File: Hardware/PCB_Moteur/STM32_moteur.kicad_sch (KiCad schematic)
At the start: 66 parts, among them J2 Conn_01x06_Pin, U2 STM32F103CBT6

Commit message: wip: new pressure et fix alim
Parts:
- removed R59: 22R, Resistor_SMD:R_0603_1608Metric, symbol Device:R_Small
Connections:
- no-connect marks 2 -> 3
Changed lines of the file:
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@@
 	)
 	(no_connect
+		(at 133.35 72.39)
+	)
+	(no_connect
 		(at 133.35 95.25)
 	)
@@
 	(wire
 		(pts
-			(xy 125.73 72.39) (xy 127 72.39)
-		)
-		(stroke
-			(width 0)
-			(type default)
-		)
-	)
-	(wire
-		(pts
 			(xy 243.84 35.56) (xy 251.46 35.56)
 		)
@@
 	(wire
 		(pts
-			(xy 132.08 72.39) (xy 133.35 72.39)
-		)
-		(stroke
-			(width 0)
-			(type default)
-		)
-	)
-	(wire
-		(pts
 			(xy 148.59 127) (xy 151.13 127)
 		)
@@
 		)
 	)
-	(global_label "Pressure_Sleep"
-		(shape input)
-		(at 125.73 72.39 180)
-		(fields_autoplaced yes)
-		(effects
-			(font
-				(size 1.27 1.27)
-			)
-			(justify right)
-		)
-		(property "Intersheetrefs" "${INTERSHEET_REFS}"
-			(at 108.3515 72.39 0)
-			(effects
-				(font
-					(size 1.27 1.27)
-				)
-				(justify right)
-				(hide yes)
-			)
-		)
-	)
 	(global_label "Servo3_Close"
 		(shape input)
@@
 					(unit 1)
 				)
-			)
-		)
-	)
-	(symbol
-		(lib_id "Device:R_Small")
-		(at 129.54 72.39 90)
-		(unit 1)
-		(exclude_from_sim no)
-		(in_bom yes)
-		(on_board yes)
-		(dnp no)
-		(property "Reference" "R59"
-			(at 102.87 72.39 90)
-			(effects
-				(font
-					(size 1.016 1.016)
-				)
-				(justify left)
-			)
-		)
-		(property "Value" "22R"
-			(at 99.314 72.39 90)
-			(effects
-				(font
-					(size 1.27 1.27)
-				)
-				(justify left)
-			)
-		)
-		(property "Footprint" "Resistor_SMD:R_0603_1608Metric"
-			(at 129.54 72.39 0)
-			(effects
-				(font
-					(size 1.27 1.27)
-				)
-				(hide yes)
-			)
-		)
-		(property "Datasheet" "~"
-			(at 129.54 72.39 0)
-			(effects
-				(font
-					(size 1.27 1.27)
-				)
-				(hide yes)
-			)
-		)
-		(property "Description" "Resistor, small symbol"
-			(at 129.54 72.39 0)
-			(effects
-				(font
-					(size 1.27 1.27)
-				)
-				(hide yes)
-			)
-		)
-		(pin "1"
-		)
-		(pin "2"
-		)
-		(instances
-			(project "PCB_moteur"
-				(path "/b0d87684-7b1c-41d8-8358-755aa327573e/753d1783-c2f5-4012-bbb8-3f4eadf066f6"
-					(reference "R59")
-					(unit 1)
-				)
-			)
-			(project "STM32_moteur"
-				(path "/da6e3e70-7434-4a0f-acc5-62316b7258e2"
-					(reference "R?")
-					(unit 1)
-				)

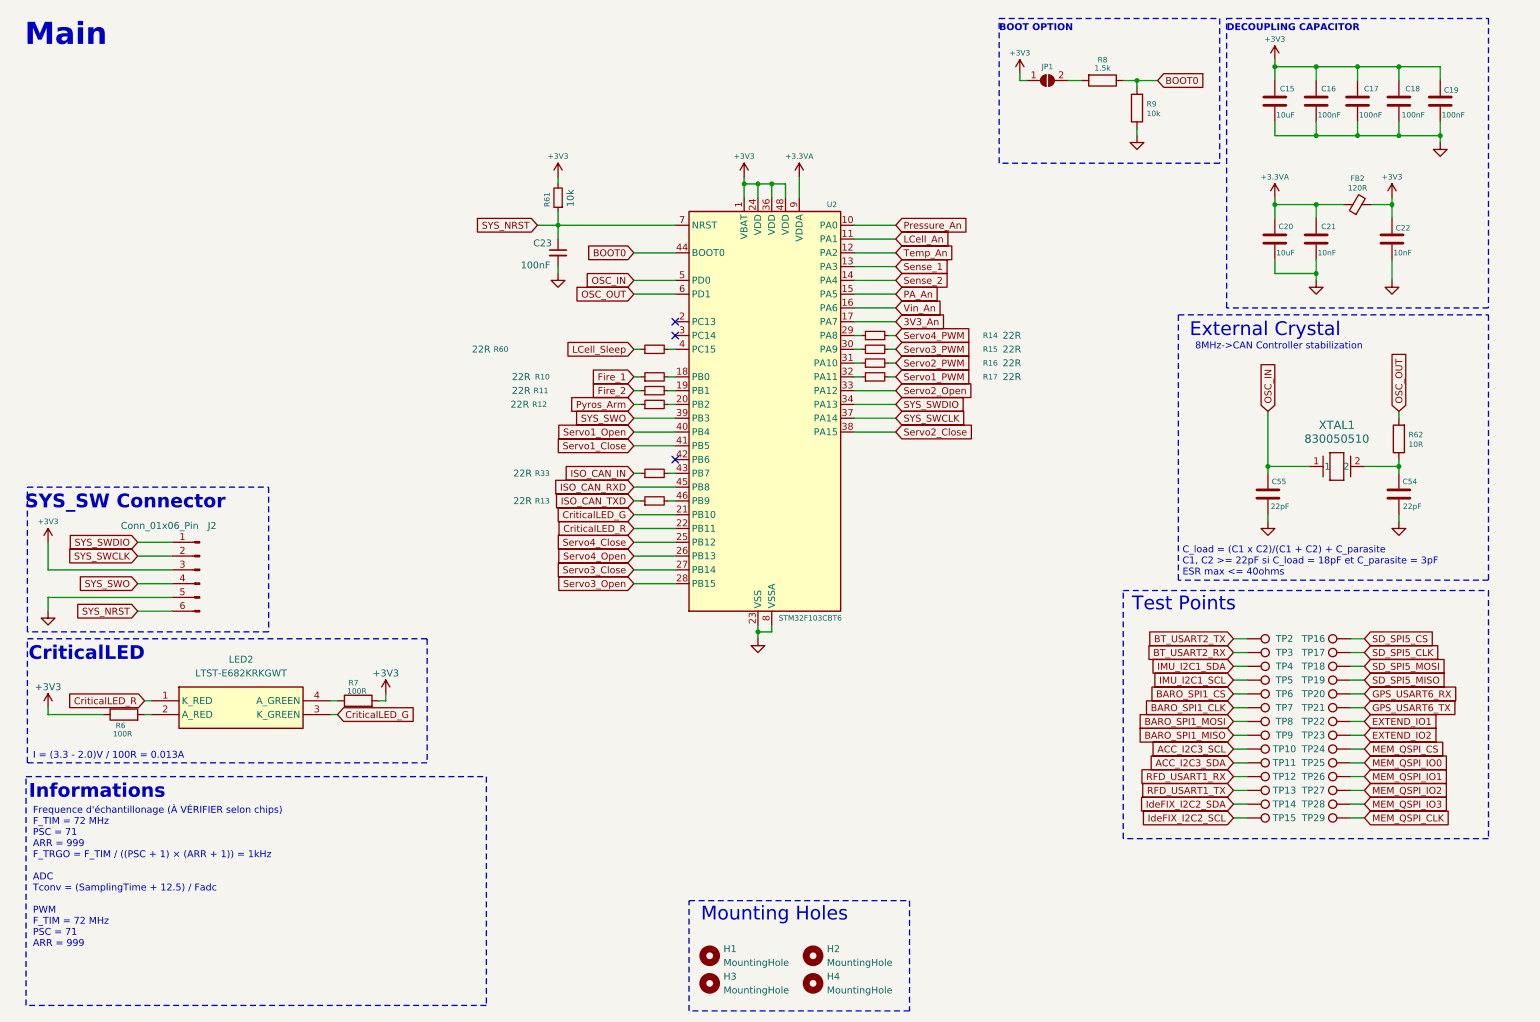
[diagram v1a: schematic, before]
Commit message: wip : work on silkscreen and add all info to BOM
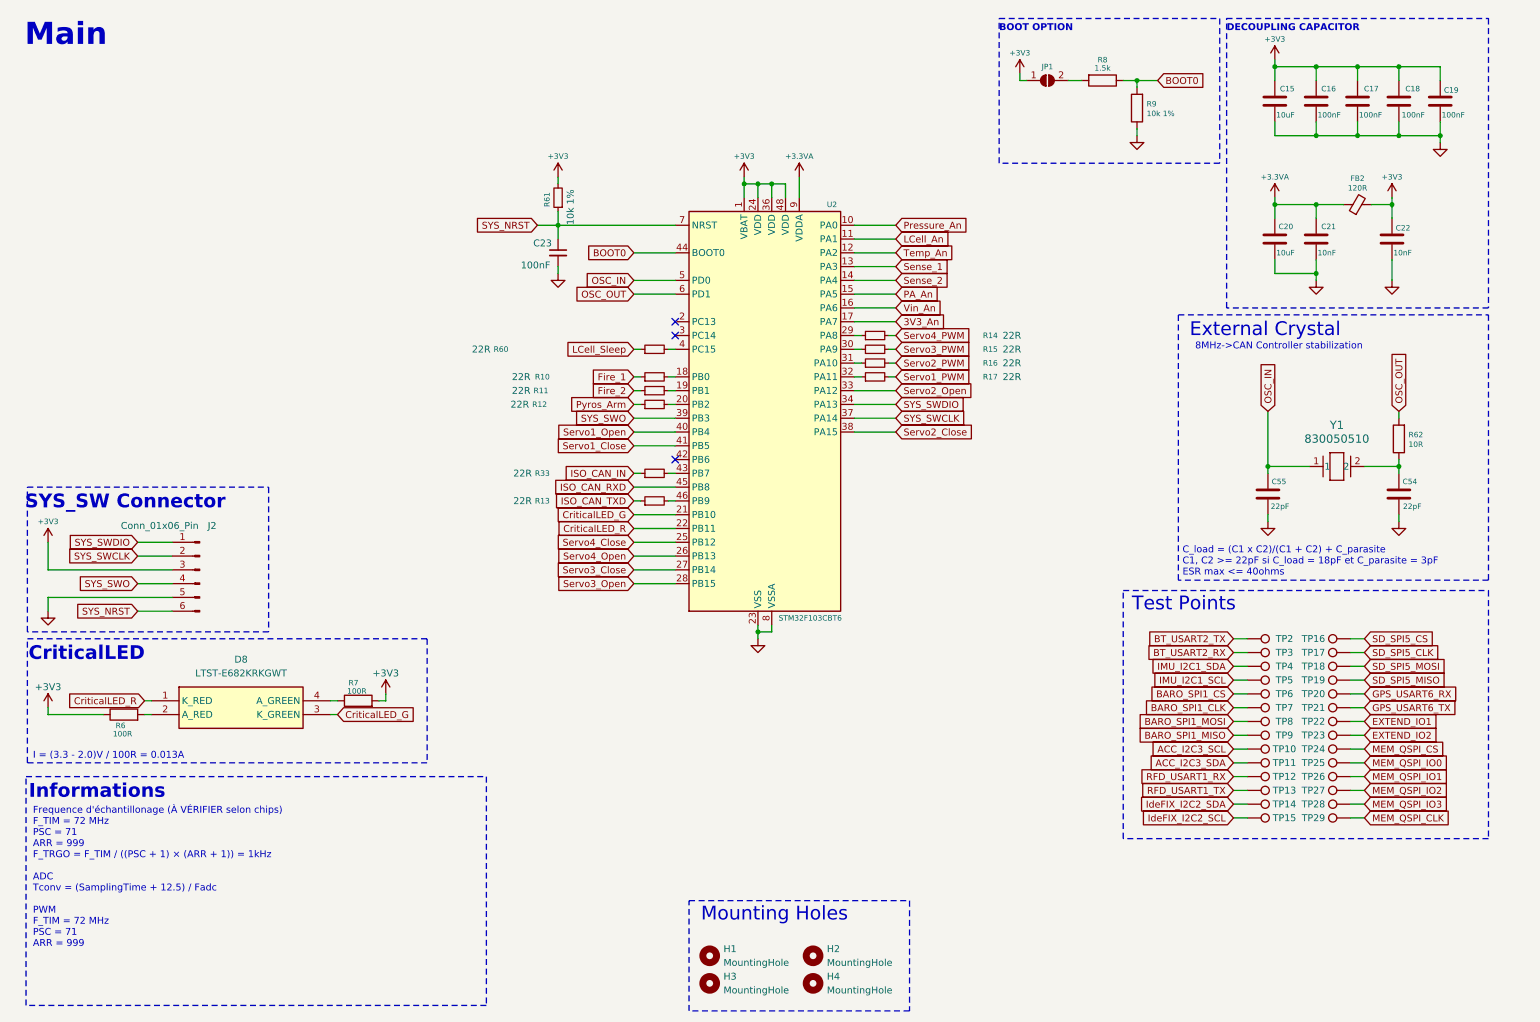
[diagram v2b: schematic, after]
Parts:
- C15, C20: DigiKey_Part_Number (none) -> 1276-2891-1-ND; Manufacturer_Part_Number (none) -> CL21A106KAYNNNE
- C16, C17, C18, C19, C23: DigiKey_Part_Number (none) -> 399-C0805C104K5RACTUCT-ND; Manufacturer_Part_Number (none) -> C0805C104K5RACTU
- C21, C22: DigiKey_Part_Number (none) -> 399-C0603C103K5RACTUCT-ND; Manufacturer_Part_Number (none) -> C0603C103K5RACTU
- D8: renamed from LED2; DigiKey_Part_Number (none) -> 160-2215-1-ND
- FB2: DigiKey_Part_Number (none) -> 1934-1472-1-ND; Manufacturer_Part_Number (none) -> 2508051217Y6
- H1, H2, H3, H4, JP1, TP10, TP11, TP12, TP13, TP14, TP15, TP16, TP17, TP18, TP19, TP2, TP20, TP21, TP22, TP23, TP24, TP25, TP26, TP27, TP28, TP29, TP3, TP4, TP5, TP6, TP7, TP8, TP9: DigiKey_Part_Number (none) -> -; Manufacturer_Part_Number (none) -> -
- J2: DigiKey_Part_Number (none) -> 732-5319-ND; Manufacturer_Part_Number (none) -> 61300611121
- R10, R11, R12, R13, R14, R15, R16, R17, R33, R60: DigiKey_Part_Number (none) -> RHM22DCT-ND; Manufacturer_Part_Number (none) -> ESR03EZPJ220
- R6, R7: DigiKey_Part_Number (none) -> 541-100CCT-ND; Manufacturer_Part_Number (none) -> CRCW0805100RFKEA
- R61: value 10k -> 10k 1%; DigiKey_Part_Number (none) -> 541-10.0KCCT-ND; Manufacturer_Part_Number (none) -> CRCW080510K0FKEA
- R62: DigiKey_Part_Number 311-10.0KHRCT-ND -> 311-10.0CRCT-ND; Manufacturer_Part_Number RC0603FR-0710KL -> RC0805FR-0710RL
- R8: footprint Resistor_SMD:R_0603_1608Metric -> Resistor_SMD:R_0805_2012Metric; DigiKey_Part_Number (none) -> P1.5KDBCT-ND; Manufacturer_Part_Number (none) -> ERA-3AEB152V
- R9: value 10k -> 10k 1%; footprint Resistor_SMD:R_0603_1608Metric -> Resistor_SMD:R_0805_2012Metric; DigiKey_Part_Number (none) -> 541-10.0KCCT-ND; Manufacturer_Part_Number (none) -> CRCW080510K0FKEA
- U2: DigiKey_Part_Number (none) -> 497-6288-ND; Manufacturer_Part_Number (none) -> STM32F103CBT6
- Y1: renamed from XTAL1; DigiKey_Part_Number (none) -> 1923-830050510CT-ND; Manufacturer_Part_Number (none) -> 830050510

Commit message: wip : reorder refdes and fix footprints
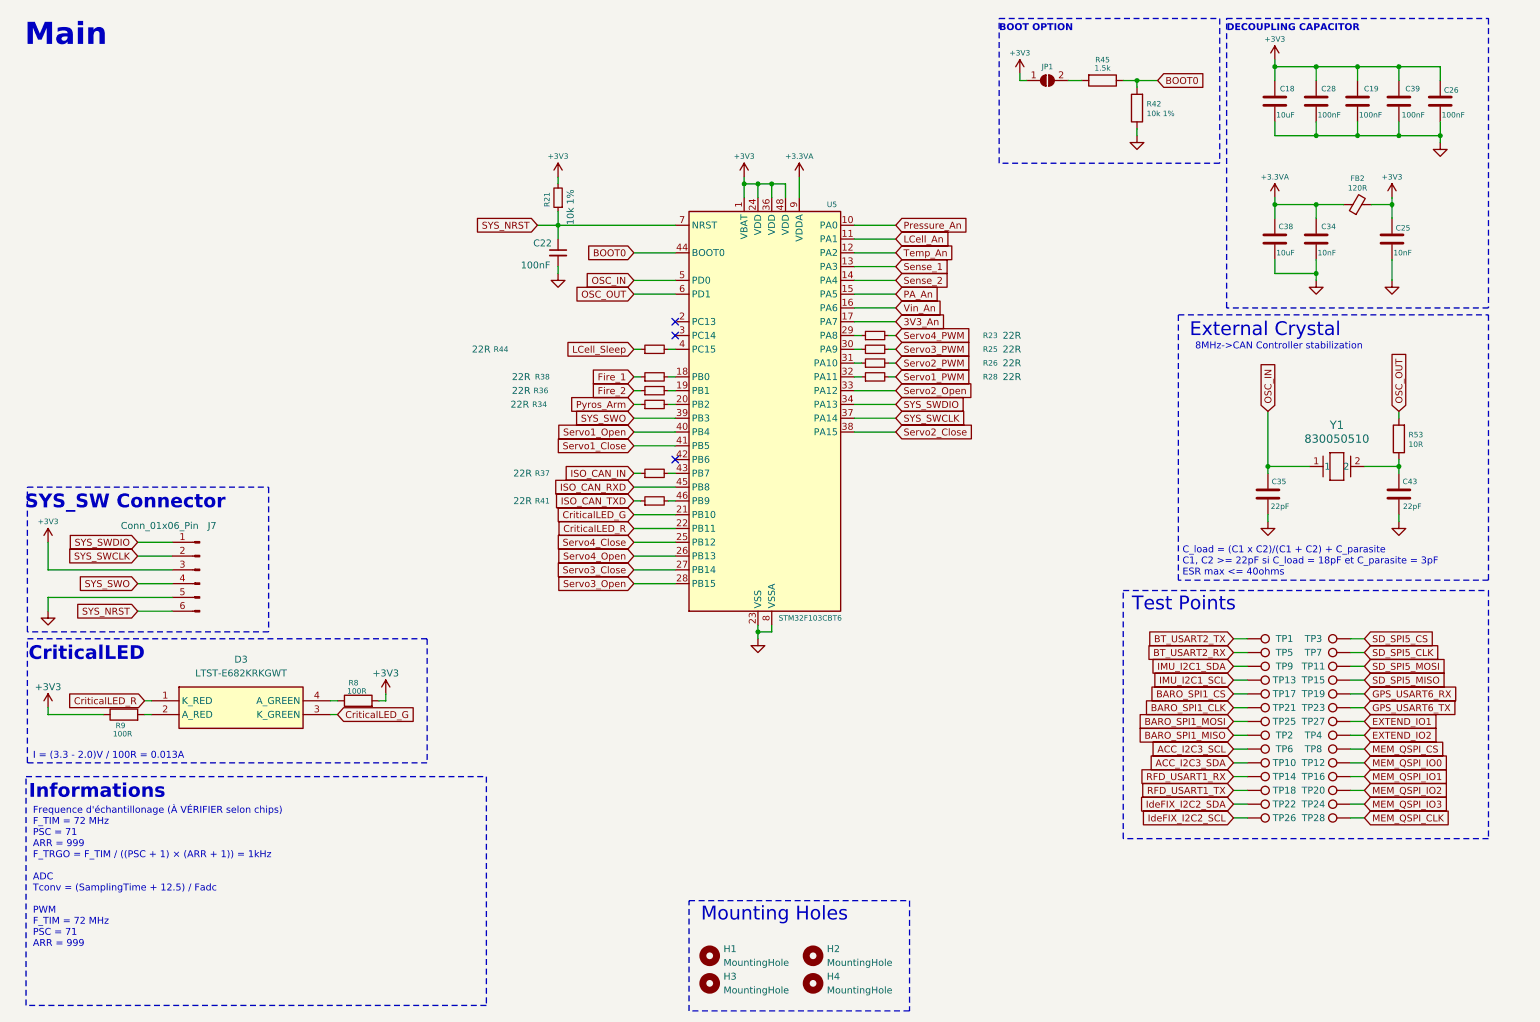
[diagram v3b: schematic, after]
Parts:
- renumbered C15 to C18, C17 to C19, C23 to C22, C22 to C25, C19 to C26, C16 to C28, C21 to C34, C55 to C35, C20 to C38, C18 to C39, C54 to C43, D8 to D3, J2 to J7, R61 to R21, R14 to R23, R15 to R25, R16 to R26, R17 to R28, R12 to R34, R11 to R36, R33 to R37, R10 to R38, R13 to R41, R9 to R42, R60 to R44, R8 to R45, R62 to R53, R7 to R8, R6 to R9, TP2 to TP1, TP11 to TP10, TP18 to TP11, TP25 to TP12, TP5 to TP13, TP12 to TP14, TP19 to TP15, TP26 to TP16, TP6 to TP17, TP13 to TP18, TP20 to TP19, TP9 to TP2, TP27 to TP20, TP7 to TP21, TP14 to TP22, TP21 to TP23, TP28 to TP24, TP8 to TP25, TP15 to TP26, TP22 to TP27, TP29 to TP28, TP16 to TP3, TP23 to TP4, TP3 to TP5, TP10 to TP6, TP17 to TP7, TP24 to TP8, TP4 to TP9, U2 to U5

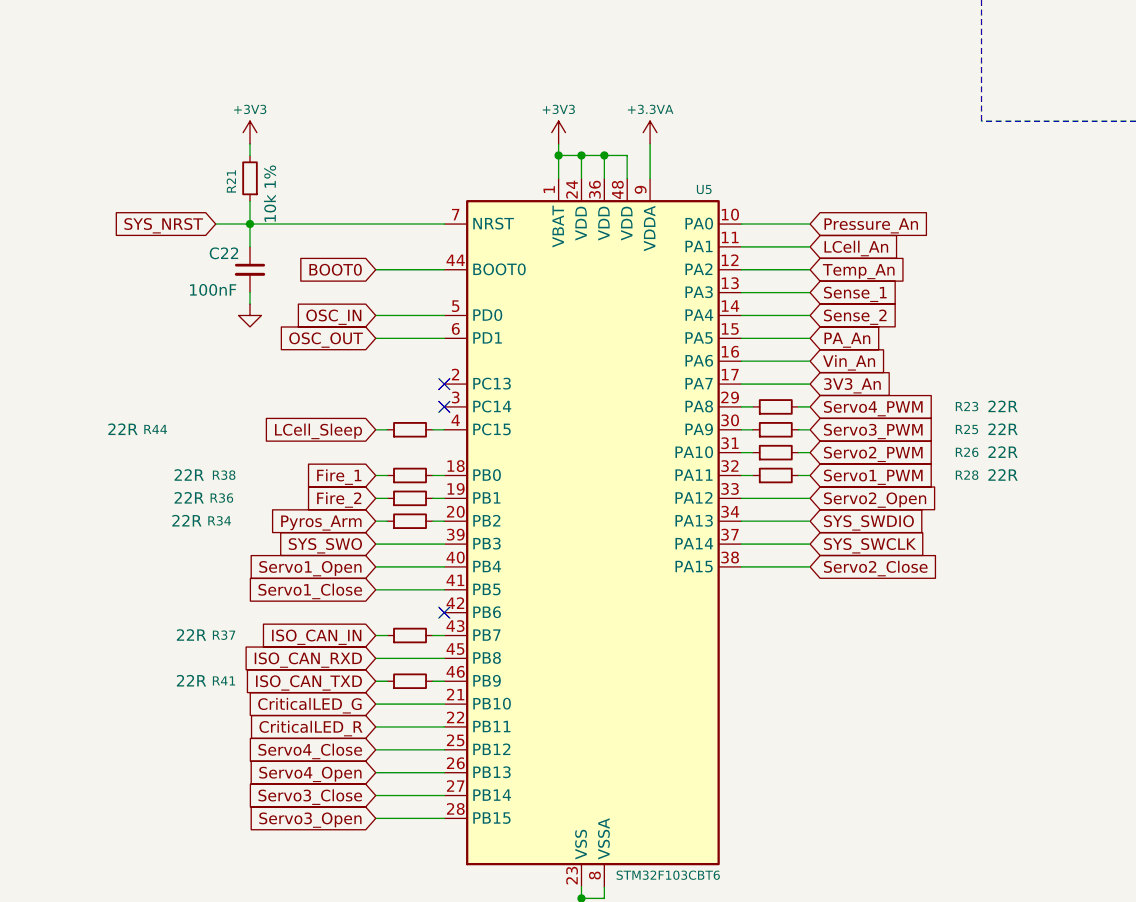
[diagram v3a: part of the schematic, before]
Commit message: fix(moteur + gse): gnd not connected for pressure sensor + seperate alim pressure sensor for motor pcb
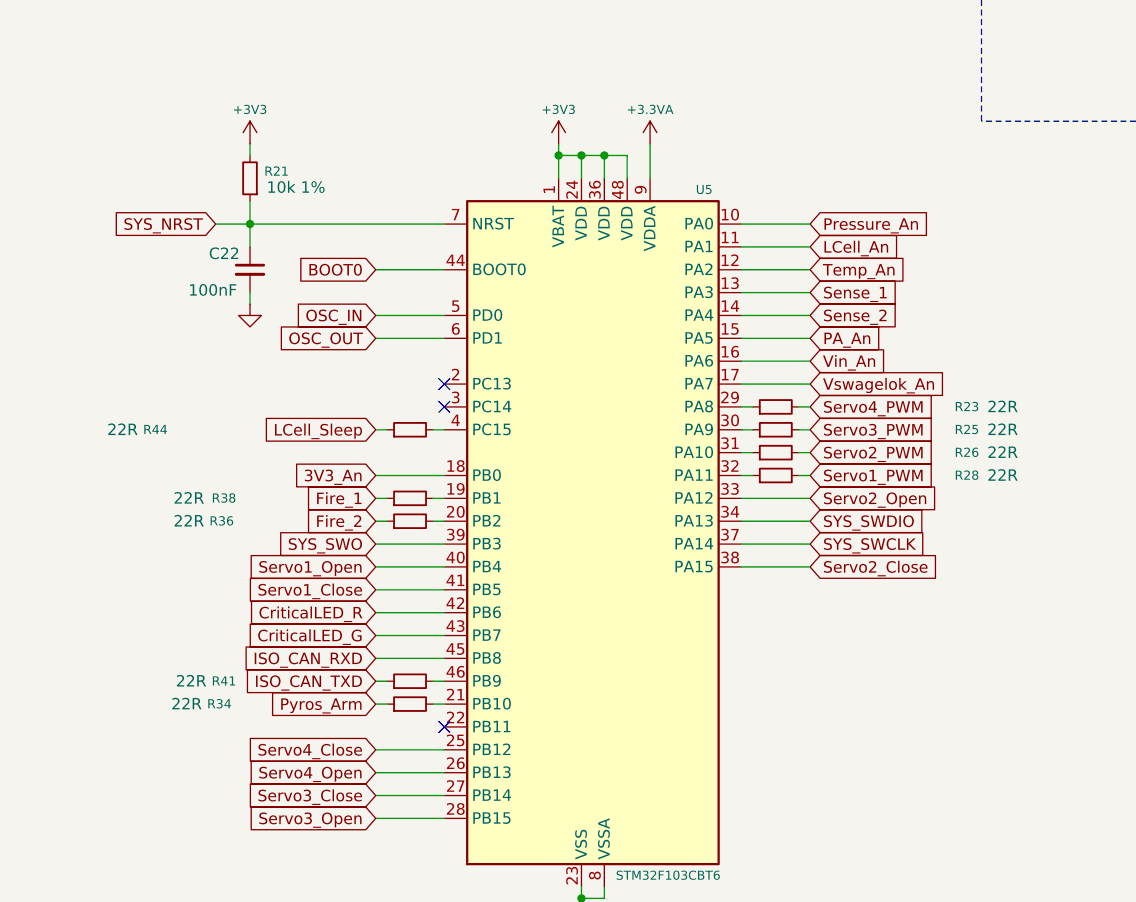
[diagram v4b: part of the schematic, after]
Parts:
- removed R37: 22R, Resistor_SMD:R_0603_1608Metric, symbol Device:R_Small
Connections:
- net 3V3_An: now also U5.18 (PB0); no longer U5.17 (PA7)
- net CriticalLED_G: now also U5.43 (PB7); no longer U5.21 (PB10)
- net CriticalLED_R: now also U5.42 (PB6); no longer U5.22 (PB11)
- net at R38.2: now also U5.19 (PB1); no longer U5.18 (PB0)
- net at R36.2: now also U5.20 (PB2); no longer U5.19 (PB1)
- net at R34.2: now also U5.21 (PB10); no longer U5.20 (PB2)
- new net Vswagelok_An: U5.17 (PA7)
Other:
- moved on the sheet: R34, R36, R38

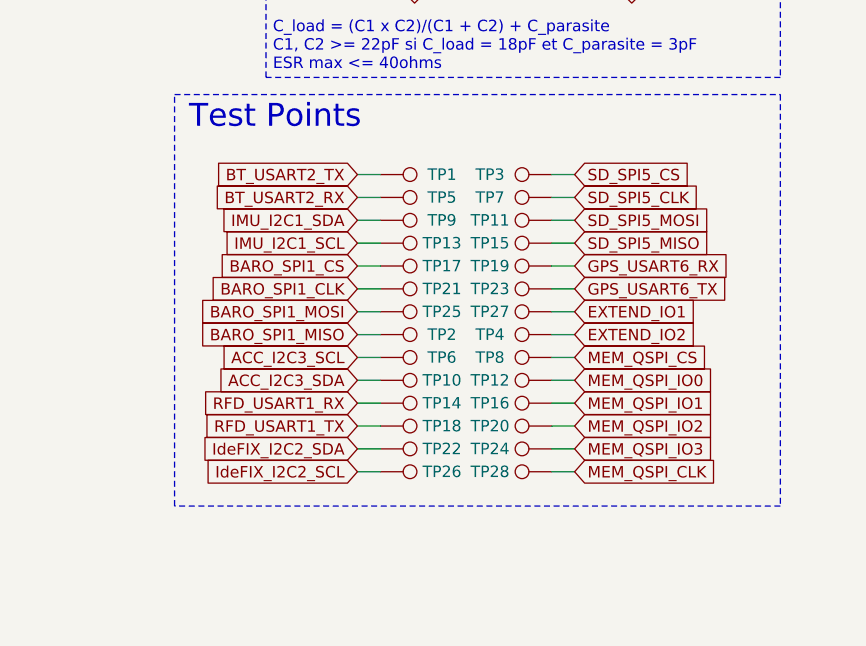
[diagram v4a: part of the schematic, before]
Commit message: wip(moteur): traces
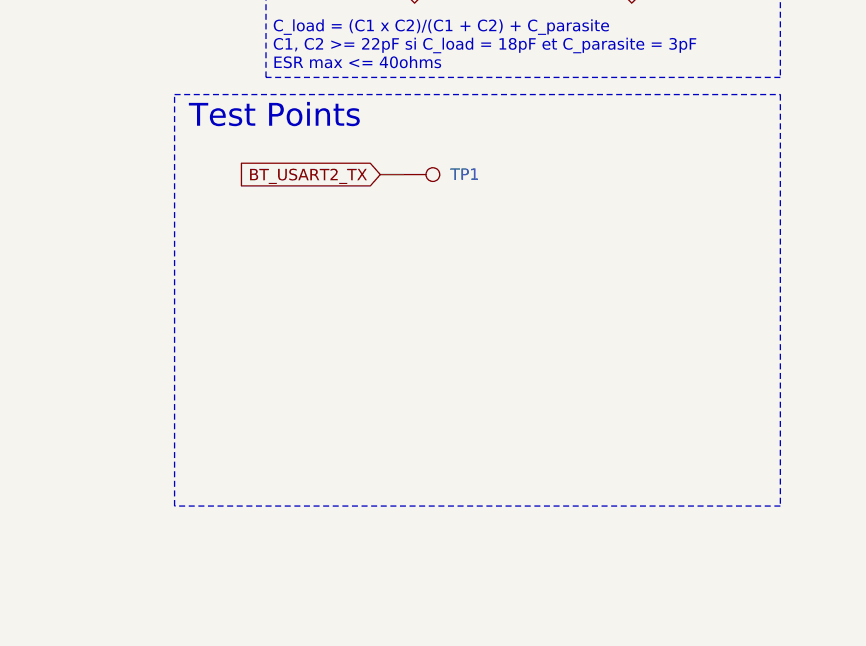
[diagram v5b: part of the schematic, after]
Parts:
- removed TP10, TP11, TP12, TP13, TP14, TP15, TP16, TP17, TP18, TP19, TP2, TP20, TP21, TP22, TP23, TP24, TP25, TP26, TP27, TP28, TP3, TP4, TP5, TP6, TP7, TP8, TP9: TestPoint, TestPoint:TestPoint_Pad_D1.0mm, symbol Connector:TestPoint
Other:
- moved on the sheet: TP1
